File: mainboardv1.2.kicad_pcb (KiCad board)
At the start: 2 copper layers, 79.7 x 80 mm, 128 parts, among them IC1 LM2596S, IC2 TDA2822D, IC3 MCP2562P, IC4 STM32F103RBT6, IC5 MIC2288YD5, IC6 ULN2003AD, IC7 LM2901, IC8 REG1117, IC9 SN74LVC1G10, Q1 8MHz

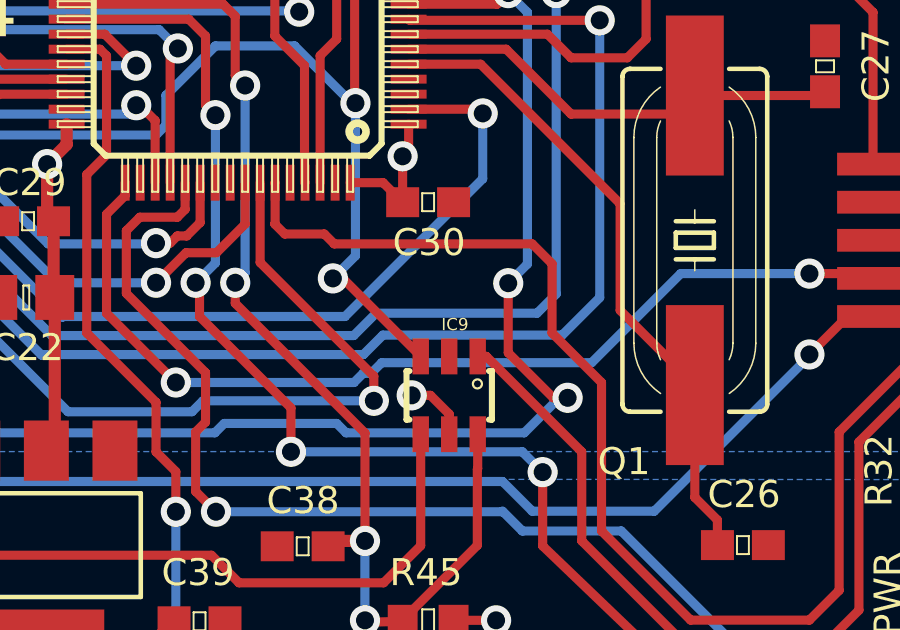
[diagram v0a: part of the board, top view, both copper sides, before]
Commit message: missed silkscreen for IC9
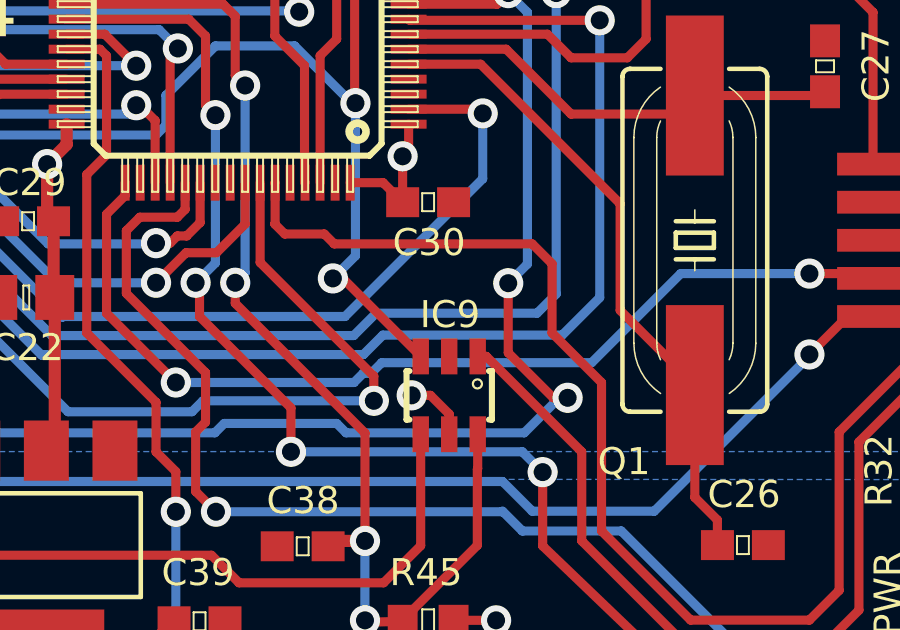
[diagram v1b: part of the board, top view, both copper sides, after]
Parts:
- ALIVE70, PWR70: footprint Mainboard_Eagle:LED_SML0805 -> Mainboard_v1.2:LED_SML0805
- C1, C2, C22, C46: footprint Mainboard_Eagle:RCL_C0805 -> Mainboard_v1.2:RCL_C0805
- C10, C11, C12, C13, C14, C15, C16, C17, C18, C19, C21, C23, C24, C25, C26, C27, C28, C29, C3, C30, C31, C32, C33, C34, C35, C36, C37, C38, C39, C4, C40, C41, C42, C43, C44, C47, C48, C5, C6, C7, C9: footprint Mainboard_Eagle:RCL_C0603 -> Mainboard_v1.2:RCL_C0603
- C20, C45: footprint Mainboard_Eagle:RCL_UD-6_3X7_7_NICHICON -> Mainboard_v1.2:RCL_UD-6_3X7_7_NICHICON
- C8: footprint Mainboard_Eagle:RCL_UD-10X10_NICHICON -> Mainboard_v1.2:RCL_UD-10X10_NICHICON
- D1, D2: footprint Mainboard_Eagle:DIODE_SMB -> Mainboard_v1.2:DIODE_SMB
- D3: footprint Mainboard_Eagle:ADAFRUIT_SOD-323F -> Mainboard_v1.2:ADAFRUIT_SOD-323F
- FID1, FID2: footprint Mainboard_Eagle:SPARKFUN-AESTHETICS_FIDUCIAL-1X2.5 -> Mainboard_v1.2:SPARKFUN-AESTHETICS_FIDUCIAL-1X2.5
- IC1: footprint Mainboard_Eagle:NATIONAL-SEMICONDUCTOR_TO263-5 -> Mainboard_v1.2:NATIONAL-SEMICONDUCTOR_TO263-5
- IC2: footprint Mainboard_Eagle:ST-MICROELECTRONICS_SO08 -> Mainboard_v1.2:ST-MICROELECTRONICS_SO08
- IC3: footprint Mainboard_Eagle:SPARKFUN-DIGITALIC_SO08 -> Mainboard_v1.2:SPARKFUN-DIGITALIC_SO08
- IC4: footprint Mainboard_Eagle:STM32_TQFP64 -> Mainboard_v1.2:STM32_TQFP64
- IC5: footprint Mainboard_Eagle:ADAFRUIT_SOT23-5L -> Mainboard_v1.2:ADAFRUIT_SOT23-5L
- IC6: footprint Mainboard_Eagle:ULN-UDN_SO16 -> Mainboard_v1.2:ULN-UDN_SO16
- IC7: footprint Mainboard_Eagle:LINEAR_SO14 -> Mainboard_v1.2:LINEAR_SO14
- IC8: footprint Mainboard_Eagle:BURR-BROWN_SOT223 -> Mainboard_v1.2:BURR-BROWN_SOT223
- IC9: footprint Mainboard_Eagle:74XX-EU_SOT23-6 -> Mainboard_v1.2:74XX-EU_SOT23-6
- JP1: footprint Mainboard_Eagle:PINHEAD_2X05_90 -> Mainboard_v1.2:PINHEAD_2X05_90
- JP2: footprint Mainboard_Eagle:PINHEAD_2X13 -> Mainboard_v1.2:PINHEAD_2X13
- JP3: footprint Mainboard_Eagle:PINHEAD_2X07 -> Mainboard_v1.2:PINHEAD_2X07
- JP6: footprint Mainboard_Eagle:CON-LEOTRONICS_1365-10 -> Mainboard_v1.2:CON-LEOTRONICS_1365-10
- JP7: footprint Mainboard_Eagle:PINHEAD_2X08 -> Mainboard_v1.2:PINHEAD_2X08
- L1, L3, L4: footprint Mainboard_Eagle:RCL_L2012C -> Mainboard_v1.2:RCL_L2012C
- L2: footprint Mainboard_Eagle:SPARKFUN-PASSIVES_CDRH125 -> Mainboard_v1.2:SPARKFUN-PASSIVES_CDRH125
- LOGO1: footprint Mainboard_Eagle:SPARKFUN-AESTHETICS_OSHW-LOGO-M -> Mainboard_v1.2:SPARKFUN-AESTHETICS_OSHW-LOGO-M
- Q1: footprint Mainboard_Eagle:CRYSTAL_HC49UP -> Mainboard_v1.2:CRYSTAL_HC49UP
- R1, R10, R11, R12, R13, R14, R15, R16, R17, R18, R19, R2, R20, R21, R22, R23, R24, R25, R26, R27, R28, R29, R3, R30, R31, R32, R33, R34, R35, R36, R37, R38, R39, R4, R40, R41, R42, R43, R44, R45, R46, R47, R48, R49, R5, R50, R51, R52, R6, R7, R8, R9: footprint Mainboard_Eagle:RCL_R0603 -> Mainboard_v1.2:RCL_R0603
- SJ1: footprint Mainboard_Eagle:SPARKFUN-PASSIVES_SJ_2S-TRACE -> Mainboard_v1.2:SPARKFUN-PASSIVES_SJ_2S-TRACE

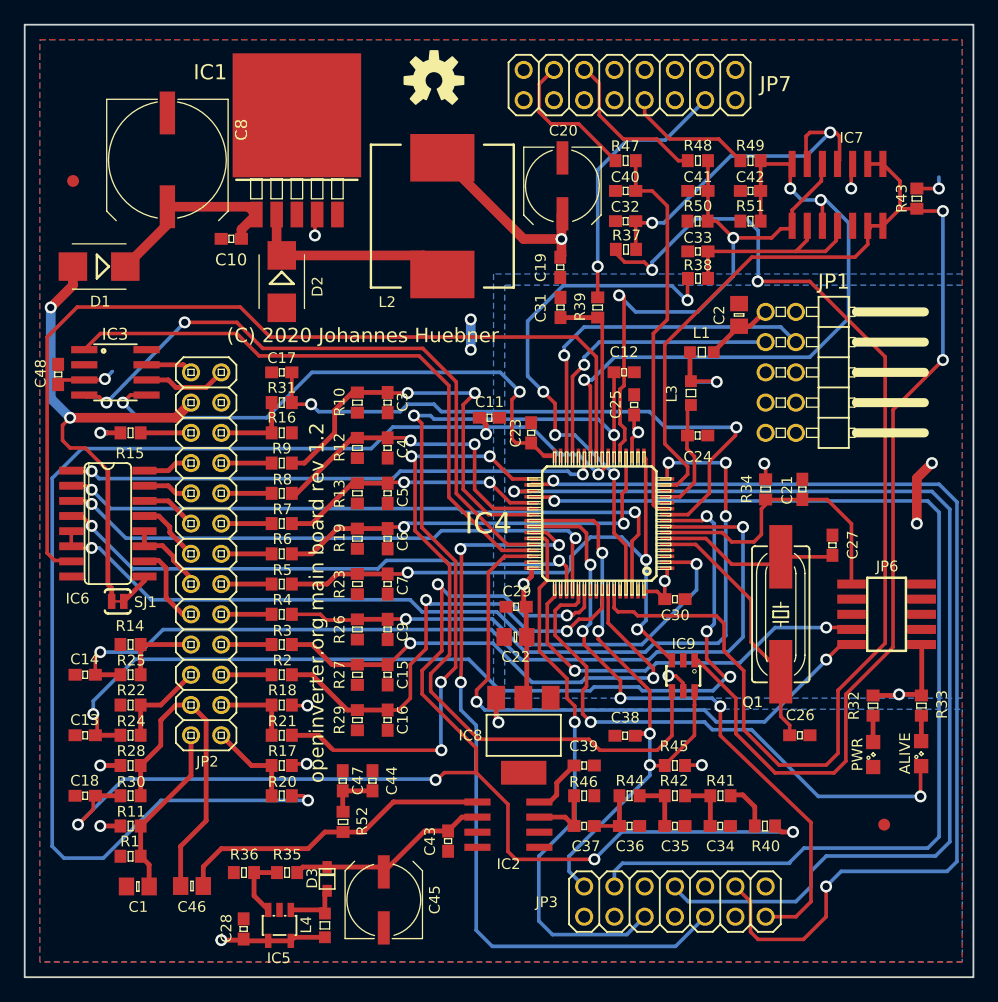
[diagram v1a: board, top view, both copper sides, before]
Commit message: mounting holes and keepout areas around
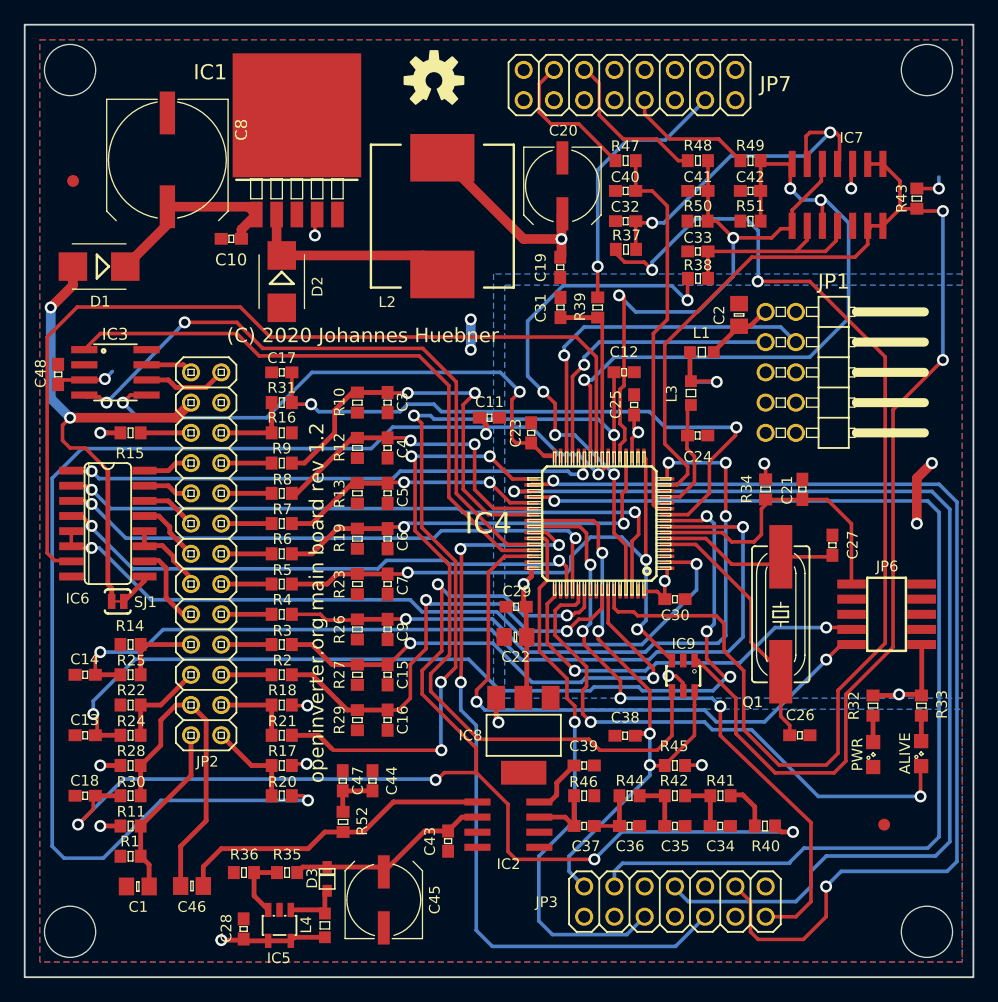
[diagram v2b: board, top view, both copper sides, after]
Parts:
- added H1: MountingHole, Mounting_Holes:MountingHole_4.3mm_M4, F.Cu at (112.5, 68.8)
- added H2: MountingHole, Mounting_Holes:MountingHole_4.3mm_M4, F.Cu at (112.5, 141.2)
- added H3: MountingHole, Mounting_Holes:MountingHole_4.3mm_M4, F.Cu at (184.4, 68.8)
- added H4: MountingHole, Mounting_Holes:MountingHole_4.3mm_M4, F.Cu at (184.4, 141.2)
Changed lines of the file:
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@@
     (tracks 1115)
     (zones 0)
-    (modules 128)
+    (modules 132)
     (nets 114)
   )
@@
       (net 4 +12V))
   )
+  (module Mounting_Holes:MountingHole_4.3mm_M4 (layer Top)
+    (at 112.4711 68.81)
+    (descr "Mounting Hole 4.3mm, no annular, M4")
+    (tags "mounting hole 4.3mm no annular m4")
+    (attr virtual)
+    (fp_text reference H1 (at 0 -5.3) (layer F.SilkS) hide
+      (effects (font (size 1 1) (thickness 0.15)))
+    )
+    (fp_text value MountingHole (at 0 5.3) (layer F.Fab)
+      (effects (font (size 1 1) (thickness 0.15)))
+    )
+    (fp_text user %R (at 0.3 0) (layer F.Fab)
+      (effects (font (size 1 1) (thickness 0.15)))
+    )
+    (fp_circle (center 0 0) (end 4.3 0) (layer Cmts.User) (width 0.15))
+    (fp_circle (center 0 0) (end 4.55 0) (layer F.CrtYd) (width 0.05))
+    (pad 1 np_thru_hole circle (at 0 0) (size 4.3 4.3) (drill 4.3) (layers *.Cu *.Mask))
+  )
+  (module Mounting_Holes:MountingHole_4.3mm_M4 (layer Top)
+    (at 112.4711 141.19)
+    (descr "Mounting Hole 4.3mm, no annular, M4")
+    (tags "mounting hole 4.3mm no annular m4")
+    (attr virtual)
+    (fp_text reference H2 (at 0 -5.3) (layer F.SilkS) hide
+      (effects (font (size 1 1) (thickness 0.15)))
+    )
+    (fp_text value MountingHole (at 0 5.3) (layer F.Fab)
+      (effects (font (size 1 1) (thickness 0.15)))
+    )
+    (fp_circle (center 0 0) (end 4.55 0) (layer F.CrtYd) (width 0.05))
+    (fp_circle (center 0 0) (end 4.3 0) (layer Cmts.User) (width 0.15))
+    (fp_text user %R (at 0.3 0) (layer F.Fab)
+      (effects (font (size 1 1) (thickness 0.15)))
+    )
+    (pad 1 np_thru_hole circle (at 0 0) (size 4.3 4.3) (drill 4.3) (layers *.Cu *.Mask))
+  )
+  (module Mounting_Holes:MountingHole_4.3mm_M4 (layer Top)
+    (at 184.44 68.81)
+    (descr "Mounting Hole 4.3mm, no annular, M4")
+    (tags "mounting hole 4.3mm no annular m4")
+    (attr virtual)
+    (fp_text reference H3 (at 0 -5.3) (layer F.SilkS) hide
+      (effects (font (size 1 1) (thickness 0.15)))
+    )
+    (fp_text value MountingHole (at 0 5.3) (layer F.Fab)
+      (effects (font (size 1 1) (thickness 0.15)))
+    )
+    (fp_text user %R (at 0.3 0) (layer F.Fab)
+      (effects (font (size 1 1) (thickness 0.15)))
+    )
+    (fp_circle (center 0 0) (end 4.3 0) (layer Cmts.User) (width 0.15))
+    (fp_circle (center 0 0) (end 4.55 0) (layer F.CrtYd) (width 0.05))
+    (pad 1 np_thru_hole circle (at 0 0) (size 4.3 4.3) (drill 4.3) (layers *.Cu *.Mask))
+  )
+  (module Mounting_Holes:MountingHole_4.3mm_M4 (layer Top)
+    (at 184.44 141.19)
+    (descr "Mounting Hole 4.3mm, no annular, M4")
+    (tags "mounting hole 4.3mm no annular m4")
+    (attr virtual)
+    (fp_text reference H4 (at 0 -5.3) (layer F.SilkS) hide
+      (effects (font (size 1 1) (thickness 0.15)))
+    )
+    (fp_text value MountingHole (at 0 5.3) (layer F.Fab)
+      (effects (font (size 1 1) (thickness 0.15)))
+    )
+    (fp_circle (center 0 0) (end 4.55 0) (layer F.CrtYd) (width 0.05))
+    (fp_circle (center 0 0) (end 4.3 0) (layer Cmts.User) (width 0.15))
+    (fp_text user %R (at 0.3 0) (layer F.Fab)
+      (effects (font (size 1 1) (thickness 0.15)))
+    )
+    (pad 1 np_thru_hole circle (at 0 0) (size 4.3 4.3) (drill 4.3) (layers *.Cu *.Mask))
+  )
   (gr_text ALIVE (at 182.6 126.2 90) (layer F.SilkS)
     (effects (font (size 0.9 0.9) (thickness 0.1)))
@@
       )
     )
+  )
+  (zone (net 0) (net_name "") (layers F&B.Cu) (hatch edge 0.508)
+    (connect_pads (clearance 0.508))
+    (min_thickness 0.254)
+    (keepout (tracks not_allowed) (vias not_allowed) (copperpour not_allowed))
+    (fill (arc_segments 16) (thermal_gap 0.508) (thermal_bridge_width 0.508))
+    (polygon
+      (pts
+        (xy 181.75 66.25) (xy 181.75 71.5) (xy 187.5 71.5) (xy 187.5 66.25)
+      )
+    )
+  )
+  (zone (net 0) (net_name "") (layers F&B.Cu) (hatch edge 0.508)
+    (connect_pads (clearance 0.508))
+    (min_thickness 0.254)
+    (keepout (tracks not_allowed) (vias not_allowed) (copperpour not_allowed))
+    (fill (arc_segments 16) (thermal_gap 0.508) (thermal_bridge_width 0.508))
+    (polygon
+      (pts
+        (xy 115 71.5) (xy 115 66.25) (xy 109.75 66.25) (xy 109.75 71.5)
+      )
+    )
+  )
+  (zone (net 0) (net_name "") (layers F&B.Cu) (hatch edge 0.508)
+    (connect_pads (clearance 0.508))
+    (min_thickness 0.254)
+    (keepout (tracks not_allowed) (vias not_allowed) (copperpour not_allowed))
+    (fill (arc_segments 16) (thermal_gap 0.508) (thermal_bridge_width 0.508))
+    (polygon
+      (pts
+        (xy 109.75 138.75) (xy 115.25 138.75) (xy 115.25 143.75) (xy 109.75 143.75)
+      )
+    )
+  )
+  (zone (net 0) (net_name "") (layers F&B.Cu) (hatch edge 0.508)
+    (connect_pads (clearance 0.508))
+    (min_thickness 0.254)
+    (keepout (tracks not_allowed) (vias not_allowed) (copperpour not_allowed))
+    (fill (arc_segments 16) (thermal_gap 0.508) (thermal_bridge_width 0.508))
+    (polygon
+      (pts
+        (xy 187.5 138.75) (xy 181.75 138.75) (xy 181.75 144) (xy 187.5 144)
+      )
+    )
